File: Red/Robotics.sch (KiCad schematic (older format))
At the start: 18 parts, among them J701 Conn_01x03, J702 Conn_01x03, J703 Screw_Terminal_01x02, J704 Screw_Terminal_01x02, Q701 DMG3414U, Q702 DMG3414U, Q703 DMG3414U, Q704 DMG3414U, Q705 DMG3414U

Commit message: Made one library in the project folder with all symbols and footprints for easy sharing
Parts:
- J704: footprint my_library:2_pin_screw_terminal -> Red:2_pin_screw_terminal
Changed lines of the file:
@@
 F 0 "J704" H 5830 4342 50  0000 L CNN
 F 1 "Screw_Terminal_01x02" H 5830 4251 50  0000 L CNN
-F 2 "my_library:2_pin_screw_terminal" H 5750 4350 50  0001 C CNN
+F 2 "Red:2_pin_screw_terminal" H 5750 4350 50  0001 C CNN
 F 3 "~" H 5750 4350 50  0001 C CNN
 F 4 "A98333-ND" H 5750 4350 50  0001 C CNN "digikey"

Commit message: updated documentation and fixed a few minor erros
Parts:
- J702: footprint my_library:WM4901-ND -> Red:WM4901-ND
- J703: footprint my_library:2_pin_screw_terminal -> Red:2_pin_screw_terminal
- R706, R708: footprint my_library:dpak_back_isolated -> Red:dpak_back_isolated
- e1: renamed from J701; footprint my_library:WM4901-ND -> Red:WM4901-ND
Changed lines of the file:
@@
 F 0 "J703" H 4830 4592 50  0000 L CNN
 F 1 "Screw_Terminal_01x02" H 4600 4400 50  0000 L CNN
-F 2 "my_library:2_pin_screw_terminal" H 4750 4600 50  0001 C CNN
+F 2 "Red:2_pin_screw_terminal" H 4750 4600 50  0001 C CNN
 F 3 "~" H 4750 4600 50  0001 C CNN
 F 4 "A98333-ND" H 4750 4600 50  0001 C CNN "digikey"
@@
 F 0 "R708" H 5620 5546 50  0000 L CNN
 F 1 "4.7" H 5620 5455 50  0000 L CNN
-F 2 "my_library:dpak_back_isolated" V 5480 5500 50  0001 C CNN
+F 2 "Red:dpak_back_isolated" V 5480 5500 50  0001 C CNN
 F 3 "~" H 5550 5500 50  0001 C CNN
 F 4 "PWR263S-20-4R70J" H 5550 5500 50  0001 C CNN "digikey"
@@
 F 0 "R706" H 4620 5546 50  0000 L CNN
 F 1 "4.7" H 4620 5455 50  0000 L CNN
-F 2 "my_library:dpak_back_isolated" V 4480 5500 50  0001 C CNN
+F 2 "Red:dpak_back_isolated" V 4480 5500 50  0001 C CNN
 F 3 "~" H 4550 5500 50  0001 C CNN
 F 4 "PWR263S-20-4R70J" H 4550 5500 50  0001 C CNN "digikey"
@@
 PWM2
 $Comp
-L Connector_Generic:Conn_01x03 J701
+L Connector_Generic:Conn_01x03 e1
 U 1 1 5ECA1558
 P 2950 3650
-F 0 "J701" H 3030 3692 50  0000 L CNN
+F 0 "e1" H 3030 3692 50  0000 L CNN
 F 1 "Conn_01x03" H 3030 3601 50  0000 L CNN
-F 2 "my_library:WM4901-ND" H 2950 3650 50  0001 C CNN
+F 2 "Red:WM4901-ND" H 2950 3650 50  0001 C CNN
 F 3 "~" H 2950 3650 50  0001 C CNN
 F 4 "WM4901-ND" H 2950 3650 50  0001 C CNN "digikey"
@@
 F 0 "J702" H 3030 5392 50  0000 L CNN
 F 1 "Conn_01x03" H 3030 5301 50  0000 L CNN
-F 2 "my_library:WM4901-ND" H 2950 5350 50  0001 C CNN
+F 2 "Red:WM4901-ND" H 2950 5350 50  0001 C CNN
 F 3 "~" H 2950 5350 50  0001 C CNN
 F 4 "WM4901-ND" H 2950 5350 50  0001 C CNN "digikey"

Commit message: Post design review
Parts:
- renumbered C701 to C301, J702 to J301, J703 to J302, J704 to J303, Q701 to Q301, Q702 to Q302, Q703 to Q303, Q704 to Q304, Q705 to Q305, R701 to R301, R702 to R302, R703 to R303, R704 to R304, R705 to R305, R706 to R306, R707 to R307, R708 to R308, e1 to e301
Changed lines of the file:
@@
 $EndDescr
 $Comp
-L Transistor_FET:DMG3414U Q704
+L Transistor_FET:DMG3414U Q304
 U 1 1 5EC3D6BF
 P 4900 3500
-F 0 "Q704" H 5104 3546 50  0000 L CNN
+F 0 "Q304" H 5104 3546 50  0000 L CNN
 F 1 "DMG3414U" H 5104 3455 50  0000 L CNN
 F 2 "Package_TO_SOT_SMD:SOT-23" H 5100 3425 50  0001 L CIN
@@
 $EndComp
 $Comp
-L power:+BATT #PWR0710
+L power:+BATT #PWR0310
 U 1 1 5EC468ED
 P 5000 3200
-F 0 "#PWR0710" H 5000 3050 50  0001 C CNN
+F 0 "#PWR0310" H 5000 3050 50  0001 C CNN
 F 1 "+BATT" H 5015 3373 50  0000 C CNN
 F 2 "" H 5000 3200 50  0001 C CNN
@@
 	5000 4350 5550 4350
 $Comp
-L Transistor_FET:DMG3414U Q703
+L Transistor_FET:DMG3414U Q303
 U 1 1 5EC4C061
 P 4450 5050
-F 0 "Q703" H 4654 5096 50  0000 L CNN
+F 0 "Q303" H 4654 5096 50  0000 L CNN
 F 1 "DMG3414U" H 4650 4900 50  0000 L CNN
 F 2 "Package_TO_SOT_SMD:SOT-23" H 4650 4975 50  0001 L CIN
@@
 $EndComp
 $Comp
-L Transistor_FET:DMG3414U Q705
+L Transistor_FET:DMG3414U Q305
 U 1 1 5EC51B7C
 P 5450 5100
-F 0 "Q705" H 5654 5146 50  0000 L CNN
+F 0 "Q305" H 5654 5146 50  0000 L CNN
 F 1 "DMG3414U" H 5654 5055 50  0000 L CNN
 F 2 "Package_TO_SOT_SMD:SOT-23" H 5650 5025 50  0001 L CIN
@@
 $EndComp
 $Comp
-L Transistor_FET:DMG3414U Q701
+L Transistor_FET:DMG3414U Q301
 U 1 1 5EC526DD
 P 1750 3300
-F 0 "Q701" H 1954 3346 50  0000 L CNN
+F 0 "Q301" H 1954 3346 50  0000 L CNN
 F 1 "DMG3414U" H 1954 3255 50  0000 L CNN
 F 2 "Package_TO_SOT_SMD:SOT-23" H 1950 3225 50  0001 L CIN
@@
 $EndComp
 $Comp
-L Transistor_FET:DMG3414U Q702
+L Transistor_FET:DMG3414U Q302
 U 1 1 5EC532D4
 P 1750 5000
-F 0 "Q702" H 1954 5046 50  0000 L CNN
+F 0 "Q302" H 1954 5046 50  0000 L CNN
 F 1 "DMG3414U" H 1954 4955 50  0000 L CNN
 F 2 "Package_TO_SOT_SMD:SOT-23" H 1950 4925 50  0001 L CIN
@@
 $EndComp
 $Comp
-L Connector:Screw_Terminal_01x02 J704
+L Connector:Screw_Terminal_01x02 J303
 U 1 1 5EC555A9
 P 5750 4350
-F 0 "J704" H 5830 4342 50  0000 L CNN
+F 0 "J303" H 5830 4342 50  0000 L CNN
 F 1 "Screw_Terminal_01x02" H 5830 4251 50  0000 L CNN
 F 2 "Red:2_pin_screw_terminal" H 5750 4350 50  0001 C CNN
@@
 $EndComp
 $Comp
-L Connector:Screw_Terminal_01x02 J703
+L Connector:Screw_Terminal_01x02 J302
 U 1 1 5EC5733C
 P 4750 4600
-F 0 "J703" H 4830 4592 50  0000 L CNN
+F 0 "J302" H 4830 4592 50  0000 L CNN
 F 1 "Screw_Terminal_01x02" H 4600 4400 50  0000 L CNN
 F 2 "Red:2_pin_screw_terminal" H 4750 4600 50  0001 C CNN
@@
 ARM
 $Comp
-L Device:R R708
+L Device:R R308
 U 1 1 5EC5E747
 P 5550 5500
-F 0 "R708" H 5620 5546 50  0000 L CNN
+F 0 "R308" H 5620 5546 50  0000 L CNN
 F 1 "4.7" H 5620 5455 50  0000 L CNN
 F 2 "Red:dpak_back_isolated" V 5480 5500 50  0001 C CNN
@@
 $EndComp
 $Comp
-L Device:R R706
+L Device:R R306
 U 1 1 5EC5F0B0
 P 4550 5500
-F 0 "R706" H 4620 5546 50  0000 L CNN
+F 0 "R306" H 4620 5546 50  0000 L CNN
 F 1 "4.7" H 4620 5455 50  0000 L CNN
 F 2 "Red:dpak_back_isolated" V 4480 5500 50  0001 C CNN
@@
 	4550 5650 4550 5750
 $Comp
-L power:GND #PWR0709
+L power:GND #PWR0309
 U 1 1 5EC60038
 P 4550 5750
-F 0 "#PWR0709" H 4550 5500 50  0001 C CNN
+F 0 "#PWR0309" H 4550 5500 50  0001 C CNN
 F 1 "GND" H 4555 5577 50  0000 C CNN
 F 2 "" H 4550 5750 50  0001 C CNN
@@
 $EndComp
 $Comp
-L Device:R R707
+L Device:R R307
 U 1 1 5EC663AF
 P 5200 5500
-F 0 "R707" H 5270 5546 50  0000 L CNN
+F 0 "R307" H 5270 5546 50  0000 L CNN
 F 1 "10k" H 5270 5455 50  0000 L CNN
 F 2 "Resistor_SMD:R_0805_2012Metric_Pad1.15x1.40mm_HandSolder" V 5130 5500 50  0001 C CNN
@@
 	5050 5100 5200 5100
 $Comp
-L Device:R R705
+L Device:R R305
 U 1 1 5EC67F75
 P 4200 5500
-F 0 "R705" H 4270 5546 50  0000 L CNN
+F 0 "R305" H 4270 5546 50  0000 L CNN
 F 1 "10k" H 4270 5455 50  0000 L CNN
 F 2 "Resistor_SMD:R_0805_2012Metric_Pad1.15x1.40mm_HandSolder" V 4130 5500 50  0001 C CNN
@@
 	5200 5650 5550 5650
 $Comp
-L power:+5V #PWR0701
+L power:+5V #PWR0301
 U 1 1 5EC840D5
 P 1850 2850
-F 0 "#PWR0701" H 1850 2700 50  0001 C CNN
+F 0 "#PWR0301" H 1850 2700 50  0001 C CNN
 F 1 "+5V" H 1865 3023 50  0000 C CNN
 F 2 "" H 1850 2850 50  0001 C CNN
@@
 $EndComp
 $Comp
-L power:+5V #PWR0703
+L power:+5V #PWR0303
 U 1 1 5EC84C41
 P 1850 4600
-F 0 "#PWR0703" H 1850 4450 50  0001 C CNN
+F 0 "#PWR0303" H 1850 4450 50  0001 C CNN
 F 1 "+5V" H 1865 4773 50  0000 C CNN
 F 2 "" H 1850 4600 50  0001 C CNN
@@
 	5200 5100 5250 5100
 $Comp
-L Device:R R702
+L Device:R R302
 U 1 1 5EC8940C
 P 1500 5500
-F 0 "R702" H 1570 5546 50  0000 L CNN
+F 0 "R302" H 1570 5546 50  0000 L CNN
 F 1 "10k" H 1570 5455 50  0000 L CNN
 F 2 "Resistor_SMD:R_0603_1608Metric_Pad1.05x0.95mm_HandSolder" V 1430 5500 50  0001 C CNN
@@
 $EndComp
 $Comp
-L Device:R R701
+L Device:R R301
 U 1 1 5EC89E87
 P 1500 3800
-F 0 "R701" H 1570 3846 50  0000 L CNN
+F 0 "R301" H 1570 3846 50  0000 L CNN
 F 1 "10k" H 1570 3755 50  0000 L CNN
 F 2 "Resistor_SMD:R_0603_1608Metric_Pad1.05x0.95mm_HandSolder" V 1430 3800 50  0001 C CNN
@@
 $EndComp
 $Comp
-L Device:R R704
+L Device:R R304
 U 1 1 5EC8A556
 P 1850 5500
-F 0 "R704" H 1920 5546 50  0000 L CNN
+F 0 "R304" H 1920 5546 50  0000 L CNN
 F 1 "10k" H 1920 5455 50  0000 L CNN
 F 2 "Resistor_SMD:R_0603_1608Metric_Pad1.05x0.95mm_HandSolder" V 1780 5500 50  0001 C CNN
@@
 $EndComp
 $Comp
-L Device:R R703
+L Device:R R303
 U 1 1 5EC8B127
 P 1850 3800
-F 0 "R703" H 1920 3846 50  0000 L CNN
+F 0 "R303" H 1920 3846 50  0000 L CNN
 F 1 "10k" H 1920 3755 50  0000 L CNN
 F 2 "Resistor_SMD:R_0603_1608Metric_Pad1.05x0.95mm_HandSolder" V 1780 3800 50  0001 C CNN
@@
 Connection ~ 1850 3950
 $Comp
-L power:GND #PWR0704
+L power:GND #PWR0304
 U 1 1 5EC91A3F
 P 1850 5750
-F 0 "#PWR0704" H 1850 5500 50  0001 C CNN
+F 0 "#PWR0304" H 1850 5500 50  0001 C CNN
 F 1 "GND" H 1855 5577 50  0000 C CNN
 F 2 "" H 1850 5750 50  0001 C CNN
@@
 $EndComp
 $Comp
-L power:GND #PWR0702
+L power:GND #PWR0302
 U 1 1 5EC920B1
 P 1850 4050
-F 0 "#PWR0702" H 1850 3800 50  0001 C CNN
+F 0 "#PWR0302" H 1850 3800 50  0001 C CNN
 F 1 "GND" H 1855 3877 50  0000 C CNN
 F 2 "" H 1850 4050 50  0001 C CNN
@@
 PWM2
 $Comp
-L Connector_Generic:Conn_01x03 e1
+L Connector_Generic:Conn_01x03 e301
 U 1 1 5ECA1558
 P 2950 3650
-F 0 "e1" H 3030 3692 50  0000 L CNN
+F 0 "e301" H 3030 3692 50  0000 L CNN
 F 1 "Conn_01x03" H 3030 3601 50  0000 L CNN
 F 2 "Red:WM4901-ND" H 2950 3650 50  0001 C CNN
@@
 $EndComp
 $Comp
-L Connector_Generic:Conn_01x03 J702
+L Connector_Generic:Conn_01x03 J301
 U 1 1 5ECA2BF5
 P 2950 5350
-F 0 "J702" H 3030 5392 50  0000 L CNN
+F 0 "J301" H 3030 5392 50  0000 L CNN
 F 1 "Conn_01x03" H 3030 5301 50  0000 L CNN
 F 2 "Red:WM4901-ND" H 2950 5350 50  0001 C CNN
@@
 $EndComp
 $Comp
-L power:+5V #PWR0705
+L power:+5V #PWR0305
 U 1 1 5ECA4245
 P 2600 3650
-F 0 "#PWR0705" H 2600 3500 50  0001 C CNN
+F 0 "#PWR0305" H 2600 3500 50  0001 C CNN
 F 1 "+5V" V 2615 3778 50  0000 L CNN
 F 2 "" H 2600 3650 50  0001 C CNN
@@
 $EndComp
 $Comp
-L power:+5V #PWR0707
+L power:+5V #PWR0307
 U 1 1 5ECA4D59
 P 2600 5350
-F 0 "#PWR0707" H 2600 5200 50  0001 C CNN
+F 0 "#PWR0307" H 2600 5200 50  0001 C CNN
 F 1 "+5V" V 2615 5478 50  0000 L CNN
 F 2 "" H 2600 5350 50  0001 C CNN
@@
 $EndComp
 $Comp
-L power:GND #PWR0708
+L power:GND #PWR0308
 U 1 1 5ECA5A2F
 P 2600 5550
-F 0 "#PWR0708" H 2600 5300 50  0001 C CNN
+F 0 "#PWR0308" H 2600 5300 50  0001 C CNN
 F 1 "GND" H 2605 5377 50  0000 C CNN
 F 2 "" H 2600 5550 50  0001 C CNN
@@
 $EndComp
 $Comp
-L power:GND #PWR0706
+L power:GND #PWR0306
 U 1 1 5ECA623F
 P 2600 3850
-F 0 "#PWR0706" H 2600 3600 50  0001 C CNN
+F 0 "#PWR0306" H 2600 3600 50  0001 C CNN
 F 1 "GND" H 2605 3677 50  0000 C CNN
 F 2 "" H 2600 3850 50  0001 C CNN
@@
 5V_PWM2
 $Comp
-L Device:CP C701
+L Device:CP C301
 U 1 1 5ECE0960
 P 5300 3950
-F 0 "C701" H 5450 3900 50  0000 C CNN
+F 0 "C301" H 5450 3900 50  0000 C CNN
 F 1 "1mF" H 5450 4050 50  0000 C CNN
 F 2 "Capacitor_THT:CP_Radial_D10.0mm_P5.00mm" H 5338 3800 50  0001 C CNN
@@
 $EndComp
 $Comp
-L power:GND #PWR0711
+L power:GND #PWR0311
 U 1 1 5ECF26EE
 P 5300 4100
-F 0 "#PWR0711" H 5300 3850 50  0001 C CNN
+F 0 "#PWR0311" H 5300 3850 50  0001 C CNN
 F 1 "GND" H 5305 3927 50  0000 C CNN
 F 2 "" H 5300 4100 50  0001 C CNN

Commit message: Swapped USBC connector out for one that was available, minor Silkscreen tweaks
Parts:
- R301, R302, R303, R304: digikey PNM0603-50KBTR-ND -> 311-10KGRCT-ND
- R305, R307: footprint Resistor_SMD:R_0805_2012Metric_Pad1.15x1.40mm_HandSolder -> Resistor_SMD:R_0603_1608Metric_Pad1.05x0.95mm_HandSolder; digikey PNM0603-50KBTR-ND -> 311-10KGRCT-ND
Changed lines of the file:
@@
 F 0 "R307" H 5270 5546 50  0000 L CNN
 F 1 "10k" H 5270 5455 50  0000 L CNN
-F 2 "Resistor_SMD:R_0805_2012Metric_Pad1.15x1.40mm_HandSolder" V 5130 5500 50  0001 C CNN
+F 2 "Resistor_SMD:R_0603_1608Metric_Pad1.05x0.95mm_HandSolder" V 5130 5500 50  0001 C CNN
 F 3 "~" H 5200 5500 50  0001 C CNN
-F 4 "PNM0603-50KBTR-ND" H 5200 5500 50  0001 C CNN "digikey"
+F 4 "311-10KGRCT-ND" H 5200 5500 50  0001 C CNN "digikey"
 	1    5200 5500
 	1    0    0    -1
@@
 F 0 "R305" H 4270 5546 50  0000 L CNN
 F 1 "10k" H 4270 5455 50  0000 L CNN
-F 2 "Resistor_SMD:R_0805_2012Metric_Pad1.15x1.40mm_HandSolder" V 4130 5500 50  0001 C CNN
+F 2 "Resistor_SMD:R_0603_1608Metric_Pad1.05x0.95mm_HandSolder" V 4130 5500 50  0001 C CNN
 F 3 "~" H 4200 5500 50  0001 C CNN
-F 4 "PNM0603-50KBTR-ND" H 4200 5500 50  0001 C CNN "digikey"
+F 4 "311-10KGRCT-ND" H 4200 5500 50  0001 C CNN "digikey"
 	1    4200 5500
 	1    0    0    -1
@@
 F 2 "Resistor_SMD:R_0603_1608Metric_Pad1.05x0.95mm_HandSolder" V 1430 5500 50  0001 C CNN
 F 3 "~" H 1500 5500 50  0001 C CNN
-F 4 "PNM0603-50KBTR-ND" H 1500 5500 50  0001 C CNN "digikey"
+F 4 "311-10KGRCT-ND" H 1500 5500 50  0001 C CNN "digikey"
 	1    1500 5500
 	1    0    0    -1
@@
 F 2 "Resistor_SMD:R_0603_1608Metric_Pad1.05x0.95mm_HandSolder" V 1430 3800 50  0001 C CNN
 F 3 "~" H 1500 3800 50  0001 C CNN
-F 4 "PNM0603-50KBTR-ND" H 1500 3800 50  0001 C CNN "digikey"
+F 4 "311-10KGRCT-ND" H 1500 3800 50  0001 C CNN "digikey"
 	1    1500 3800
 	1    0    0    -1
@@
 F 2 "Resistor_SMD:R_0603_1608Metric_Pad1.05x0.95mm_HandSolder" V 1780 5500 50  0001 C CNN
 F 3 "~" H 1850 5500 50  0001 C CNN
-F 4 "PNM0603-50KBTR-ND" H 1850 5500 50  0001 C CNN "digikey"
+F 4 "311-10KGRCT-ND" H 1850 5500 50  0001 C CNN "digikey"
 	1    1850 5500
 	1    0    0    -1
@@
 F 2 "Resistor_SMD:R_0603_1608Metric_Pad1.05x0.95mm_HandSolder" V 1780 3800 50  0001 C CNN
 F 3 "~" H 1850 3800 50  0001 C CNN
-F 4 "PNM0603-50KBTR-ND" H 1850 3800 50  0001 C CNN "digikey"
+F 4 "311-10KGRCT-ND" H 1850 3800 50  0001 C CNN "digikey"
 	1    1850 3800
 	1    0    0    -1

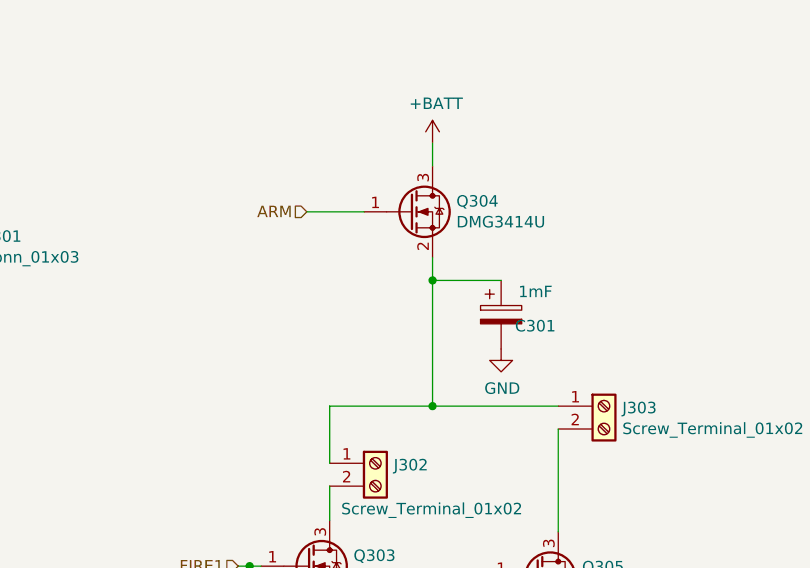
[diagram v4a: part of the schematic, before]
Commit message: Created schematic changes for Red V1.1
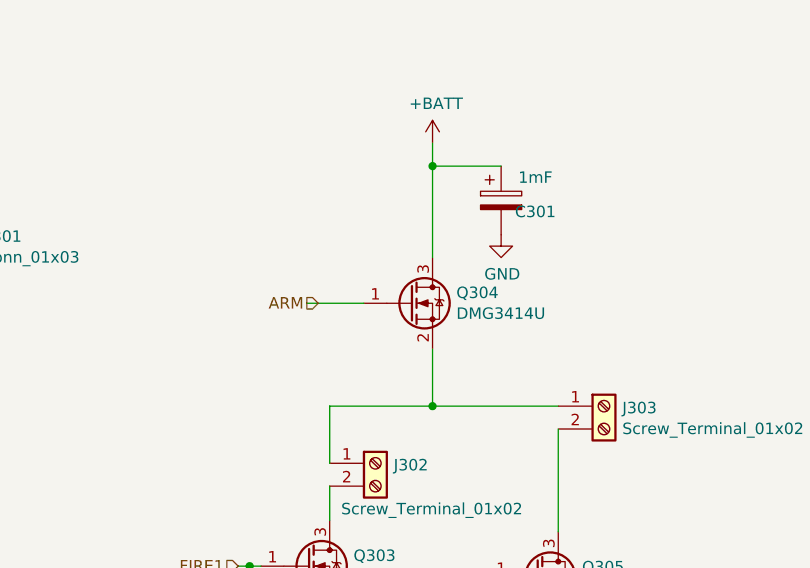
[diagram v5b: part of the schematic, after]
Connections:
- net +BATT: now also C301.1
- net at J302.1 (Pin_1), J303.1 (Pin_1), Q304.2 (S): no longer C301.1
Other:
- moved on the sheet: C301, Q304
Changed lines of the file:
@@
 L Transistor_FET:DMG3414U Q304
 U 1 1 5EC3D6BF
-P 4900 3500
-F 0 "Q304" H 5104 3546 50  0000 L CNN
-F 1 "DMG3414U" H 5104 3455 50  0000 L CNN
-F 2 "Package_TO_SOT_SMD:SOT-23" H 5100 3425 50  0001 L CIN
-F 3 "http://www.diodes.com/assets/Datasheets/ds31739.pdf" H 4900 3500 50  0001 L CNN
-F 4 "DMN1019USN-7DICT-ND" H 4900 3500 50  0001 C CNN "digikey"
-	1    4900 3500
+P 4900 3900
+F 0 "Q304" H 5104 3946 50  0000 L CNN
+F 1 "DMG3414U" H 5104 3855 50  0000 L CNN
+F 2 "Package_TO_SOT_SMD:SOT-23" H 5100 3825 50  0001 L CIN
+F 3 "http://www.diodes.com/assets/Datasheets/ds31739.pdf" H 4900 3900 50  0001 L CNN
+F 4 "DMN1019USN-7DICT-ND" H 4900 3900 50  0001 C CNN "digikey"
+	1    4900 3900
 	1    0    0    -1
 $EndComp
@@
 	5000 3200 5000 3300
 Wire Wire Line
-	4700 3500 4450 3500
+	4700 3900 4450 3900
 Wire Wire Line
 	5000 4350 5550 4350
@@
 Text HLabel 4150 5050 0    50   Input ~ 0
 FIRE1
-Text HLabel 4450 3500 0    50   Input ~ 0
+Text HLabel 4500 3900 0    50   Input ~ 0
 ARM
 $Comp
@@
 L Device:CP C301
 U 1 1 5ECE0960
-P 5300 3950
-F 0 "C301" H 5450 3900 50  0000 C CNN
-F 1 "1mF" H 5450 4050 50  0000 C CNN
-F 2 "Capacitor_THT:CP_Radial_D10.0mm_P5.00mm" H 5338 3800 50  0001 C CNN
-F 3 "~" H 5300 3950 50  0001 C CNN
-F 4 "1189-3703-1-ND" H 5300 3950 50  0001 C CNN "digikey"
-	1    5300 3950
+P 5300 3450
+F 0 "C301" H 5450 3400 50  0000 C CNN
+F 1 "1mF" H 5450 3550 50  0000 C CNN
+F 2 "Capacitor_THT:CP_Radial_D10.0mm_P5.00mm" H 5338 3300 50  0001 C CNN
+F 3 "~" H 5300 3450 50  0001 C CNN
+F 4 "1189-3703-1-ND" H 5300 3450 50  0001 C CNN "digikey"
+	1    5300 3450
 	1    0    0    -1
 $EndComp
@@
 L power:GND #PWR0311
 U 1 1 5ECF26EE
-P 5300 4100
-F 0 "#PWR0311" H 5300 3850 50  0001 C CNN
-F 1 "GND" H 5305 3927 50  0000 C CNN
-F 2 "" H 5300 4100 50  0001 C CNN
-F 3 "" H 5300 4100 50  0001 C CNN
-	1    5300 4100
-	1    0    0    -1
-$EndComp
-Wire Wire Line
-	5000 3700 5000 3800
-Wire Wire Line
-	5300 3800 5000 3800
-Connection ~ 5000 3800
-Wire Wire Line
-	5000 3800 5000 4350
+P 5300 3600
+F 0 "#PWR0311" H 5300 3350 50  0001 C CNN
+F 1 "GND" H 5305 3427 50  0000 C CNN
+F 2 "" H 5300 3600 50  0001 C CNN
+F 3 "" H 5300 3600 50  0001 C CNN
+	1    5300 3600
+	1    0    0    -1
+$EndComp
+Wire Wire Line
+	5300 3300 5000 3300
+Wire Wire Line
+	5000 4100 5000 4350
+Wire Wire Line
+	5000 3700 5000 3300
+Connection ~ 5000 3300
 $EndSCHEMATC

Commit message: Fixed a footprint error for the 32k clk
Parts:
- R306, R308: footprint Red:dpak_back_isolated -> Package_TO_SOT_SMD:TO-263-2_TabPin1
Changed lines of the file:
@@
 Text HLabel 4500 3900 0    50   Input ~ 0
 ARM
-$Comp
-L Device:R R308
-U 1 1 5EC5E747
-P 5550 5500
-F 0 "R308" H 5620 5546 50  0000 L CNN
-F 1 "4.7" H 5620 5455 50  0000 L CNN
-F 2 "Red:dpak_back_isolated" V 5480 5500 50  0001 C CNN
-F 3 "~" H 5550 5500 50  0001 C CNN
-F 4 "PWR263S-20-4R70J" H 5550 5500 50  0001 C CNN "digikey"
-	1    5550 5500
-	1    0    0    -1
-$EndComp
-$Comp
-L Device:R R306
-U 1 1 5EC5F0B0
-P 4550 5500
-F 0 "R306" H 4620 5546 50  0000 L CNN
-F 1 "4.7" H 4620 5455 50  0000 L CNN
-F 2 "Red:dpak_back_isolated" V 4480 5500 50  0001 C CNN
-F 3 "~" H 4550 5500 50  0001 C CNN
-F 4 "PWR263S-20-4R70J" H 4550 5500 50  0001 C CNN "digikey"
-	1    4550 5500
-	1    0    0    -1
-$EndComp
 Wire Wire Line
 	4550 5650 4550 5750
@@
 	5000 3700 5000 3300
 Connection ~ 5000 3300
+$Comp
+L Device:R R308
+U 1 1 5EEF6278
+P 5550 5500
+F 0 "R308" H 5620 5546 50  0000 L CNN
+F 1 "4.7" H 5620 5455 50  0000 L CNN
+F 2 "Package_TO_SOT_SMD:TO-263-2_TabPin1" V 5480 5500 50  0001 C CNN
+F 3 "~" H 5550 5500 50  0001 C CNN
+F 4 "PWR263S-20-4R70J" H 5550 5500 50  0001 C CNN "digikey"
+	1    5550 5500
+	1    0    0    -1
+$EndComp
+$Comp
+L Device:R R306
+U 1 1 5EEF8DBF
+P 4550 5500
+F 0 "R306" H 4620 5546 50  0000 L CNN
+F 1 "4.7" H 4620 5455 50  0000 L CNN
+F 2 "Package_TO_SOT_SMD:TO-263-2_TabPin1" V 4480 5500 50  0001 C CNN
+F 3 "~" H 4550 5500 50  0001 C CNN
+F 4 "PWR263S-20-4R70J" H 4550 5500 50  0001 C CNN "digikey"
+	1    4550 5500
+	1    0    0    -1
+$EndComp
 $EndSCHEMATC

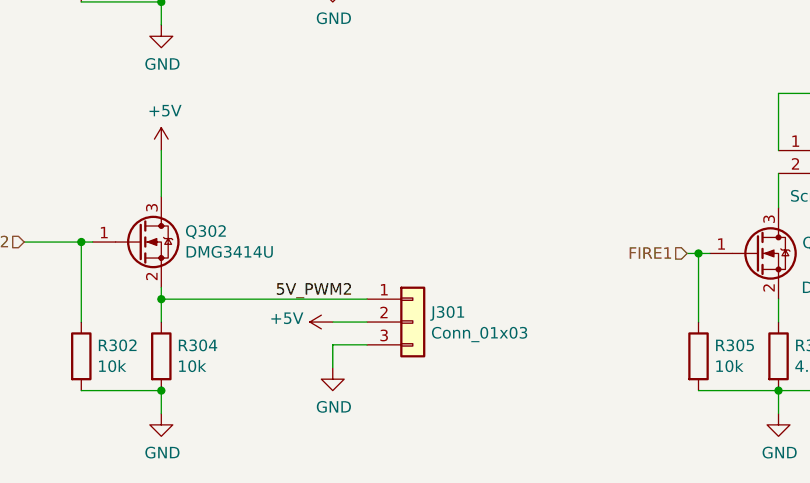
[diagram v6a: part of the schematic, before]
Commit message: Created V1.1 Layout, minor schematic updates
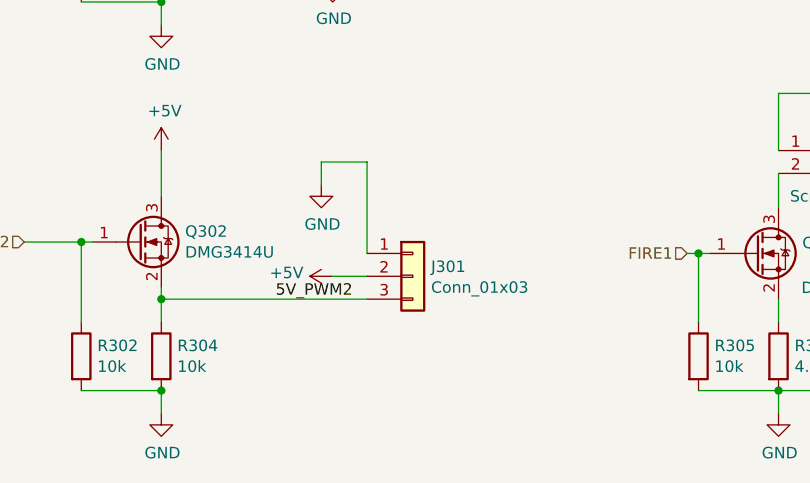
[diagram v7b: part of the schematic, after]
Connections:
- net 5V_PWM2: now also J301.3 (Pin_3); no longer J301.1 (Pin_1)
- net GND: now also J301.1 (Pin_1); no longer J301.3 (Pin_3)
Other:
- moved on the sheet: J301
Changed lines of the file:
@@
 L Connector_Generic:Conn_01x03 J301
 U 1 1 5ECA2BF5
-P 2950 5350
-F 0 "J301" H 3030 5392 50  0000 L CNN
-F 1 "Conn_01x03" H 3030 5301 50  0000 L CNN
-F 2 "Red:WM4901-ND" H 2950 5350 50  0001 C CNN
-F 3 "~" H 2950 5350 50  0001 C CNN
-F 4 "WM4901-ND" H 2950 5350 50  0001 C CNN "digikey"
-	1    2950 5350
+P 2950 5150
+F 0 "J301" H 3030 5192 50  0000 L CNN
+F 1 "Conn_01x03" H 3030 5101 50  0000 L CNN
+F 2 "Red:WM4901-ND" H 2950 5150 50  0001 C CNN
+F 3 "~" H 2950 5150 50  0001 C CNN
+F 4 "WM4901-ND" H 2950 5150 50  0001 C CNN "digikey"
+	1    2950 5150
 	1    0    0    -1
 $EndComp
@@
 L power:+5V #PWR0307
 U 1 1 5ECA4D59
-P 2600 5350
-F 0 "#PWR0307" H 2600 5200 50  0001 C CNN
-F 1 "+5V" V 2615 5478 50  0000 L CNN
-F 2 "" H 2600 5350 50  0001 C CNN
-F 3 "" H 2600 5350 50  0001 C CNN
-	1    2600 5350
+P 2600 5150
+F 0 "#PWR0307" H 2600 5000 50  0001 C CNN
+F 1 "+5V" V 2615 5278 50  0000 L CNN
+F 2 "" H 2600 5150 50  0001 C CNN
+F 3 "" H 2600 5150 50  0001 C CNN
+	1    2600 5150
 	0    -1   -1   0
 $EndComp
@@
 L power:GND #PWR0308
 U 1 1 5ECA5A2F
-P 2600 5550
-F 0 "#PWR0308" H 2600 5300 50  0001 C CNN
-F 1 "GND" H 2605 5377 50  0000 C CNN
-F 2 "" H 2600 5550 50  0001 C CNN
-F 3 "" H 2600 5550 50  0001 C CNN
-	1    2600 5550
+P 2550 4750
+F 0 "#PWR0308" H 2550 4500 50  0001 C CNN
+F 1 "GND" H 2555 4577 50  0000 C CNN
+F 2 "" H 2550 4750 50  0001 C CNN
+F 3 "" H 2550 4750 50  0001 C CNN
+	1    2550 4750
 	1    0    0    -1
 $EndComp
@@
 	2600 3750 2600 3850
 Wire Wire Line
-	2750 5350 2600 5350
+	2750 5150 2600 5150
 Wire Wire Line
-	2600 5550 2600 5450
-Wire Wire Line
-	2600 5450 2750 5450
+	2550 4750 2550 4650
 Text Label 2350 3550 0    50   ~ 0
 5V_PWM1
@@
 	1    0    0    -1
 $EndComp
+Wire Wire Line
+	2750 5050 2750 4650
+Wire Wire Line
+	2550 4650 2750 4650
 $EndSCHEMATC
